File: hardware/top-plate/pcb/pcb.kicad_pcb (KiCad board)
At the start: 2 copper layers, 130 x 130 mm, 104 parts, among them J1 Conn_01x02, SW1 SS-12D10L5, SW2 TS4535TP 250GF 009, SW3 TS4535TP 250GF 009

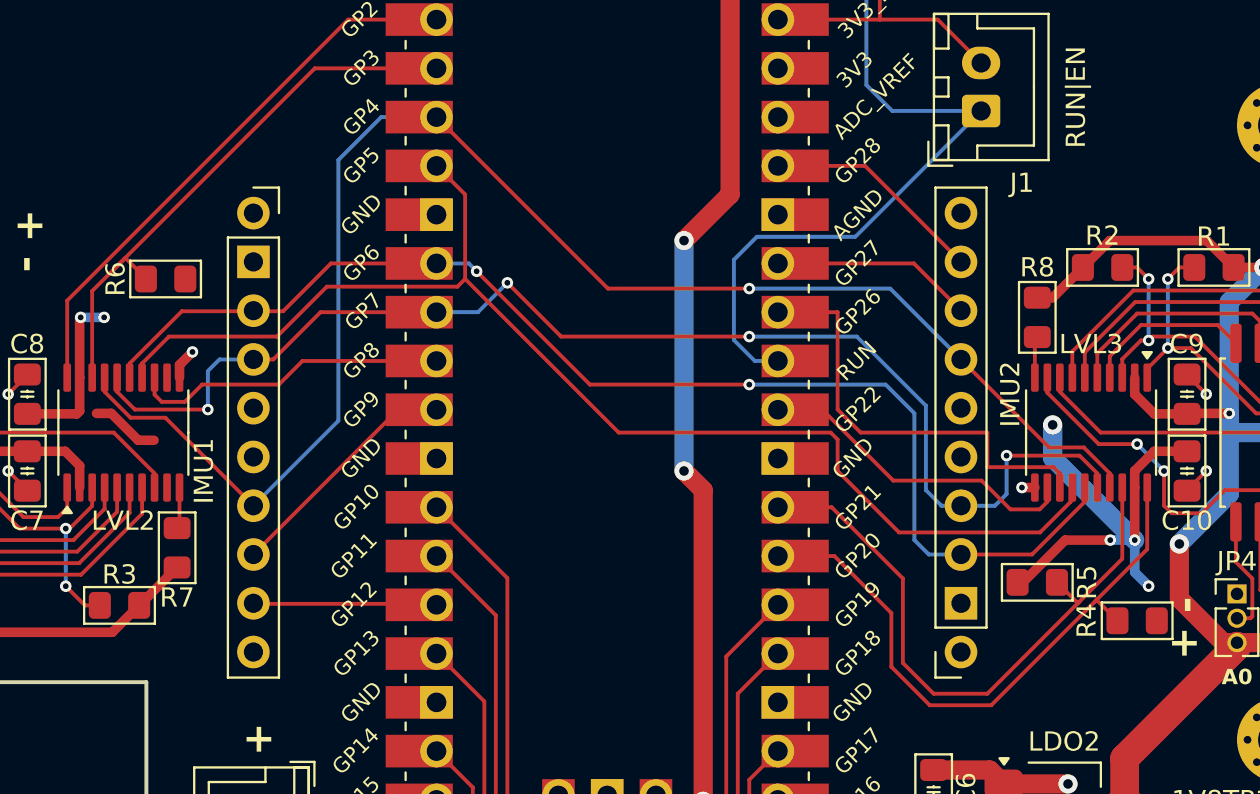
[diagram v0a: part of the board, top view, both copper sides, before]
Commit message: fixed up top pcb (icm20948 and oled were overlapping)
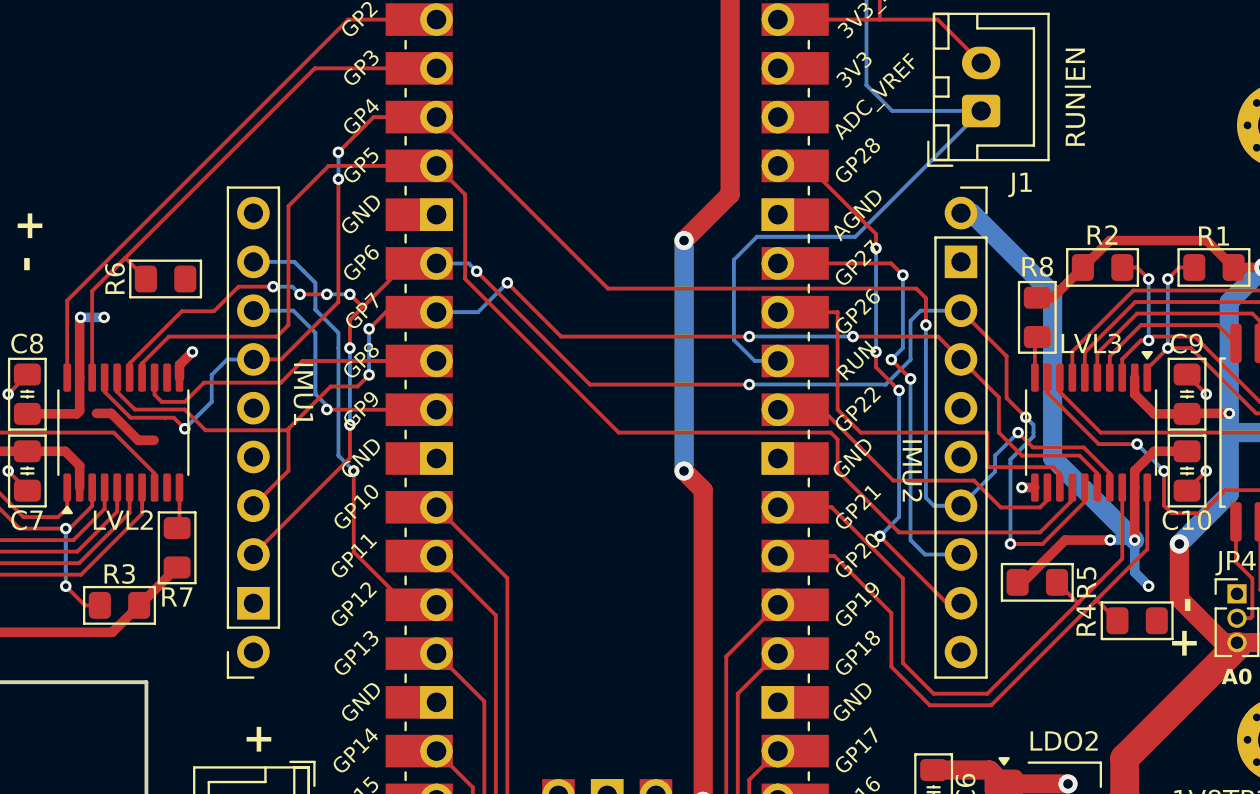
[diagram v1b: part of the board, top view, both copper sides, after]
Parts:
- moved IMU1 12.9 mm to (-24.9, 0.00), turned to 180 degrees
- moved IMU2 12.9 mm to (24.9, 0.00), turned to 0 degrees
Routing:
- net /SPI0.SCLK: track 64.7 -> 87.5 mm, vias 2 -> 10
- net /IMU2.NCS: track 11.6 -> 28.9 mm, vias 0 -> 4
- net /IMU1.NCS: track 9.53 -> 24.0 mm, vias 0 -> 1
- net /IMU2.INT: track 10.5 -> 24.2 mm, vias 0 -> 3
- net +3V3: track 55.2 -> 68.6 mm, vias 8 -> 7
- net /DMUX_SCS: track 65.3 -> 69.9 mm
- net /SPI0.MISO: track 80.4 -> 84.2 mm, vias 1 -> 5
- net /IMU1.INT: track 12.7 -> 15.7 mm, vias 0 -> 1
- net /SPI0.MOSI: track 66.9 -> 68.0 mm, vias 4 -> 5
